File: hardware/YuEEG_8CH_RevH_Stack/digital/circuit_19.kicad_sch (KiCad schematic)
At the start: 5 parts

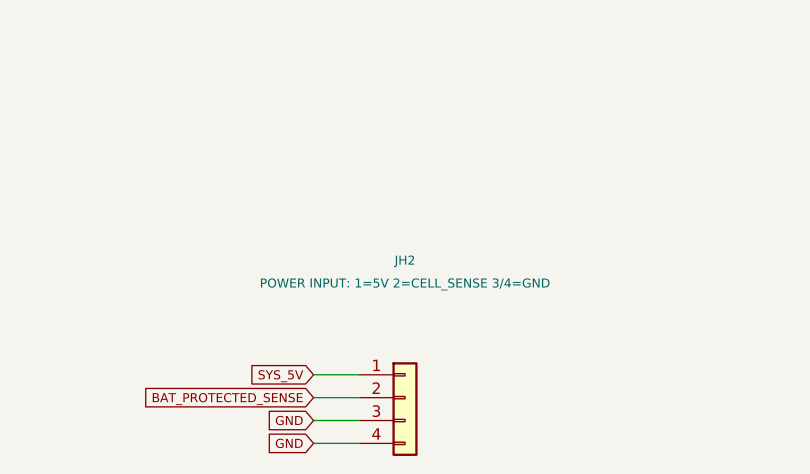
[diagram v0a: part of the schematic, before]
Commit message: Route right-facing PH4 power entry and review stacked cable clearance
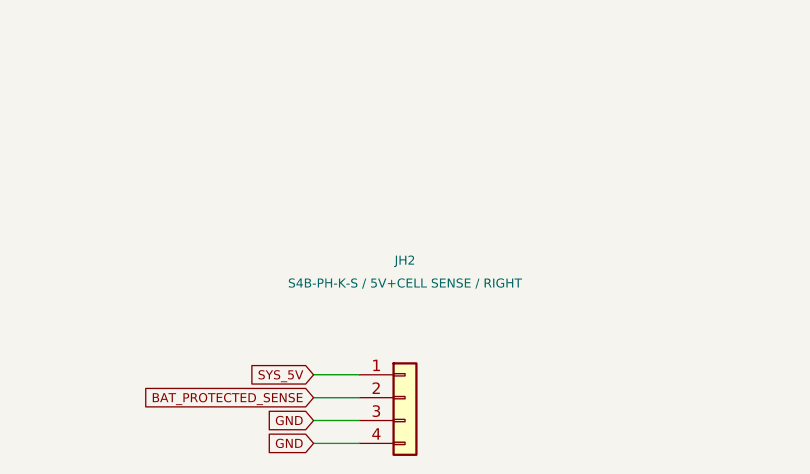
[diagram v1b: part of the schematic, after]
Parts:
- JH2: value POWER INPUT: 1=5V 2=CELL_SENSE 3/4=GND -> S4B-PH-K-S / 5V+CELL SENSE / RIGHT; footprint Connector_JST:JST_PH_S4B-PH-SM4-TB_1x04-1MP_P2.00mm_Horizontal -> Connector_JST:JST_PH_S4B-PH-K_1x04_P2.00mm_Horizontal
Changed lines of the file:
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@@
 (property
 "Value"
-"POWER INPUT: 1=5V 2=CELL_SENSE 3/4=GND"
+"S4B-PH-K-S / 5V+CELL SENSE / RIGHT"
 (at
 101.6
@@
 (property
 "Footprint"
-"Connector_JST:JST_PH_S4B-PH-SM4-TB_1x04-1MP_P2.00mm_Horizontal"
+"Connector_JST:JST_PH_S4B-PH-K_1x04_P2.00mm_Horizontal"
 (at
 101.6
@@
 (property
 "Datasheet"
-"~"
+"https://www.jst-mfg.com/product/pdf/eng/ePH.pdf"
 (at
 101.6
